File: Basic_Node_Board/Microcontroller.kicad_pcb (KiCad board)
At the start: 2 copper layers, 17 parts, among them J4 Conn_01x02_Pin, U2 ESP32-DEVKIT-C, U6 TJA1050T/CM,118

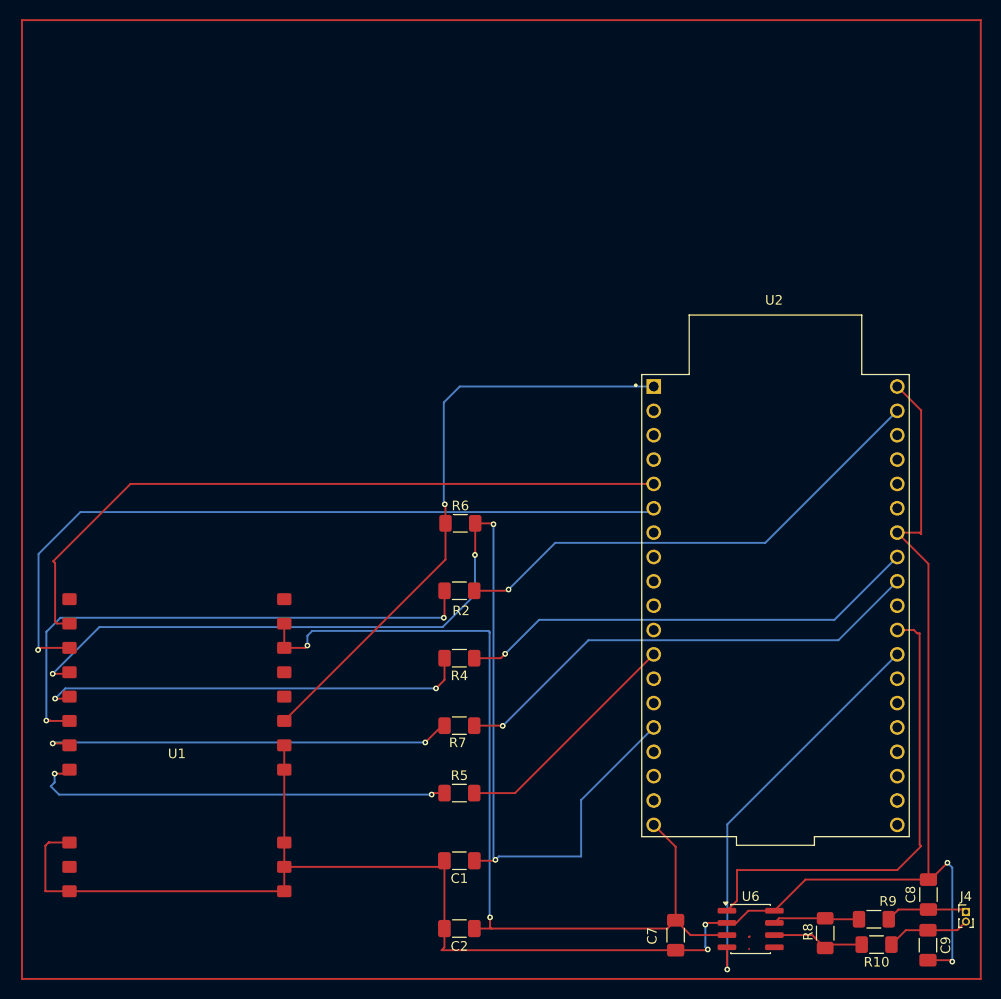
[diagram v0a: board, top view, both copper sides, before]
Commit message: microcontroller board without the buck converter yet
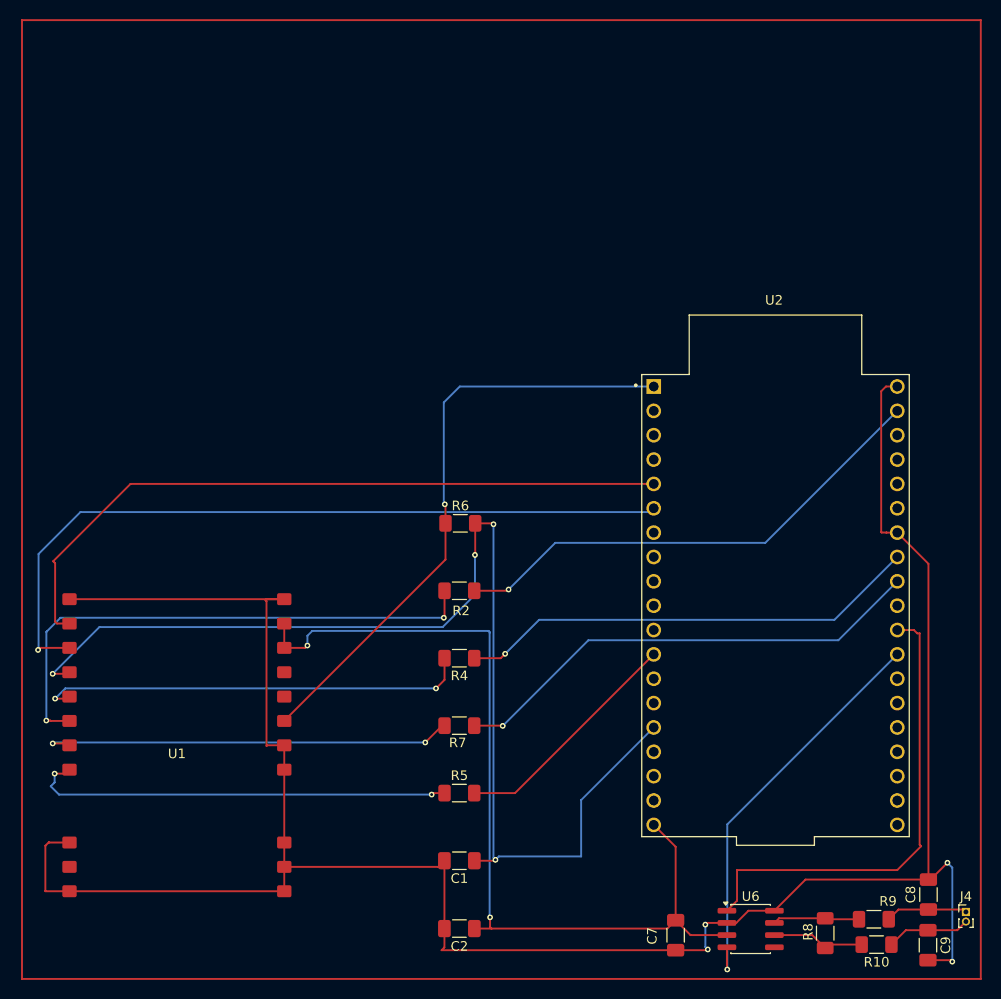
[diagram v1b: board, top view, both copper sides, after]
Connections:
- U1 pad 12: unconnected-(U1-GND-Pad12) -> GND
- U1 pad 7: unconnected-(U1-T/R_CTRL-Pad7) -> Net-(U1-DIO2)
- U1 pad 8: unconnected-(U1-DIO2-Pad8) -> Net-(U1-DIO2)
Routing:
- net GND: track 202.2 -> 243.1 mm

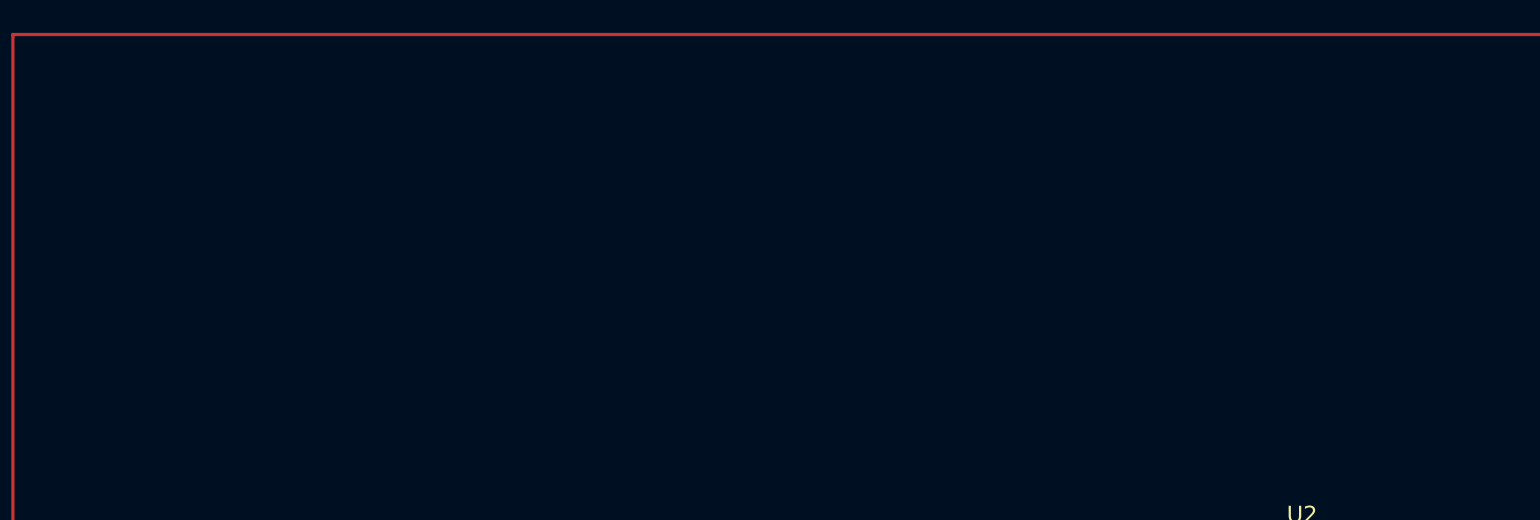
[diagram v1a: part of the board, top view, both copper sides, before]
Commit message: add buck buck converter step down to the pcb (not wirted yet)
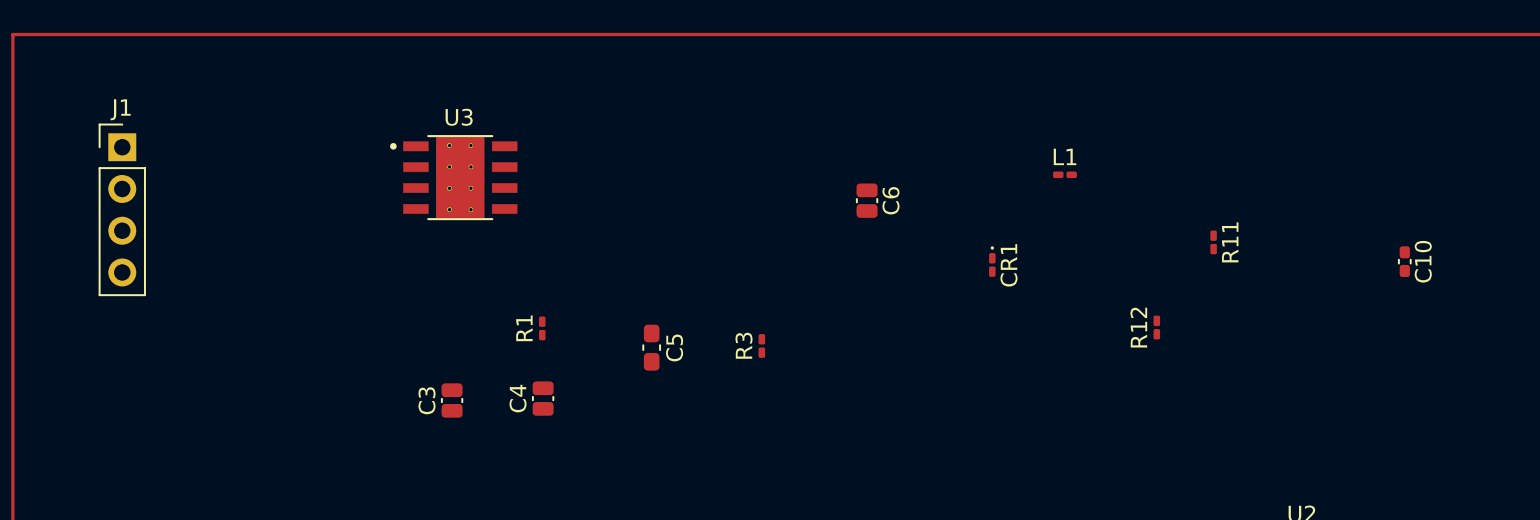
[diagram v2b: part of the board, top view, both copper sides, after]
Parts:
- added C10: 10TPE47MAZB, Capacitor_SMD:C_0402_1005Metric_Pad0.74x0.62mm_HandSolder, F.Cu at (120.2, 38.5)
- added C3: GRM31CR71H475KA12L, Capacitor_SMD:C_0504_1310Metric_Pad0.83x1.28mm_HandSolder, F.Cu at (62.2, 47.0)
- added C4: C0805C122J5GACTU, Capacitor_SMD:C_0504_1310Metric_Pad0.83x1.28mm_HandSolder, F.Cu at (67.8, 46.8)
- added C5: CL05C110JB5NNNC, Capacitor_SMD:C_0603_1608Metric_Pad1.08x0.95mm_HandSolder, F.Cu at (74.4, 43.7)
- added C6: 08053C104KAT2A, Capacitor_SMD:C_0504_1310Metric_Pad0.83x1.28mm_HandSolder, F.Cu at (87.5, 34.8)
- added CR1: B560C-13-F, Diode_SMD:D_0201_0603Metric_Pad0.64x0.40mm_HandSolder, F.Cu at (95.1, 38.7)
- added J1: Conn_01x02, Connector_PinHeader_2.54mm:PinHeader_1x04_P2.54mm_Vertical, F.Cu at (42.2, 31.5)
- added L1: SRN8040-100M, Inductor_SMD:L_0201_0603Metric_Pad0.64x0.40mm_HandSolder, F.Cu at (99.5, 33.2)
- added R1: RC0201FR-0723K7L, Resistor_SMD:R_0201_0603Metric_Pad0.64x0.40mm_HandSolder, F.Cu at (67.7, 42.6)
- added R11: CRCW040261K9FKED, Resistor_SMD:R_0201_0603Metric_Pad0.64x0.40mm_HandSolder, F.Cu at (108.6, 37.3)
- added R12: CRCW040211K0FKED, Resistor_SMD:R_0201_0603Metric_Pad0.64x0.40mm_HandSolder, F.Cu at (105.1, 42.5)
- added R3: CRCW0402118KFKED, Resistor_SMD:R_0201_0603Metric_Pad0.64x0.40mm_HandSolder, F.Cu at (81.1, 43.6)
- added U3: TPS54560BQDDARQ1, PROVE-footprints:VREG_LM5017MR_NOPB, F.Cu at (62.7, 33.4)

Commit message: beta test with all connections for final pcb layout - JK
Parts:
- added C11: 47uF, Capacitor_SMD:C_0402_1005Metric_Pad0.74x0.62mm_HandSolder, F.Cu at (79.9, 33.3)
- C10: value 10TPE47MAZB -> 47uF
- C3: value GRM31CR71H475KA12L -> 30uF
- C4: value C0805C122J5GACTU -> 82nF
- C5: value CL05C110JB5NNNC -> 100pF
- J1: footprint Connector_PinHeader_2.54mm:PinHeader_1x04_P2.54mm_Vertical -> Connector_PinHeader_1.00mm:PinHeader_1x02_P1.00mm_Vertical
- L1: value SRN8040-100M -> 47uH
- R1: value RC0201FR-0723K7L -> 5.1k
- R11: value CRCW040261K9FKED -> 10k
- R12: value CRCW040211K0FKED -> 56.2k
- R3: value CRCW0402118KFKED -> 243k
- moved J4 115.2 mm to (40.0, 51.0), turned to 180 degrees
- moved C9 111.1 mm to (46.9, 47.5), turned to 90 degrees
- moved C8 101.9 mm to (46.8, 57.1), turned to -90 degrees
- moved R10 101.3 mm to (52.5, 50.0), turned to 0 degrees
- moved R9 94.2 mm to (52.5, 57.5), turned to 0 degrees
- moved R8 91.4 mm to (57.6, 52.5), turned to 90 degrees
- moved U6 81.8 mm to (65.4, 51.9), turned to 180 degrees
- moved C7 73.1 mm to (75.0, 52.8)
- moved C10 44.2 mm to (76.3, 33.2)
- moved R3 30.7 mm to (52.5, 32.5)
- moved CR1 26.4 mm to (69.0, 34.5)
- moved C3 24.8 mm to (45.1, 29.1)
- moved C4 24.2 mm to (45.6, 37.3), turned to 0 degrees
- moved L1 23.8 mm to (76.0, 29.0), turned to 180 degrees
- moved C5 23.7 mm to (51.8, 36.5)
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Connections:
- C2 pad 1: /BUCK_5V -> 5.3V OUT
- C7 pad 2: /BUCK_5V -> 5.3V OUT
- R11 pad 1: 5.3V OUT -> Net-(U3-FB)
- R11 pad 2: Net-(U3-FB) -> GND
- R12 pad 1: GND -> Net-(U3-FB)
- R12 pad 2: Net-(U3-FB) -> 5.3V OUT
- U1 pad 10: /BUCK_5V -> 5.3V OUT
- U1 pad 9: /BUCK_5V -> 5.3V OUT
- U2 pad 19: /BUCK_5V -> 5.3V OUT
- U3 pad 3: unconnected-(U3-EN-Pad3) -> /24V
- U6 pad 3: /BUCK_5V -> 5.3V OUT
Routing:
- net GND: track 243.1 -> 422.2 mm, vias 4 -> 10
- net 5.3V OUT: track 0.00 -> 176.0 mm, vias 0 -> 4
- net /BUCK_5V: track 95.1 -> 0.00 mm, vias 2 -> 0
- net Net-(J3-Pin_12): track 42.5 -> 120.4 mm, vias 1 -> 0
- net Net-(J3-Pin_8): track 48.5 -> 94.2 mm
- net Net-(U3-FB): track 0.00 -> 31.2 mm, vias 0 -> 2
- net Net-(J3-Pin_9): track 50.4 -> 77.8 mm
- net Net-(U3-COMP): track 0.00 -> 23.9 mm
- net /24V: track 0.00 -> 22.0 mm
- net Net-(J2-Pin_5): track 73.9 -> 93.6 mm, vias 0 -> 2
- net Net-(U3-SW): track 0.00 -> 18.5 mm
- net Net-(J3-Pin_11): track 49.7 -> 65.5 mm, vias 0 -> 1
- net Net-(J2-Pin_12): track 24.7 -> 39.6 mm
- net Net-(J3-Pin_2): track 51.9 -> 65.9 mm
- net Net-(U3-BOOT): track 0.00 -> 12.2 mm
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- added copper zone on In1.Cu, net 5.3V OUT
- added copper zone on In2.Cu, net GND
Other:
- copper layers 2 -> 4

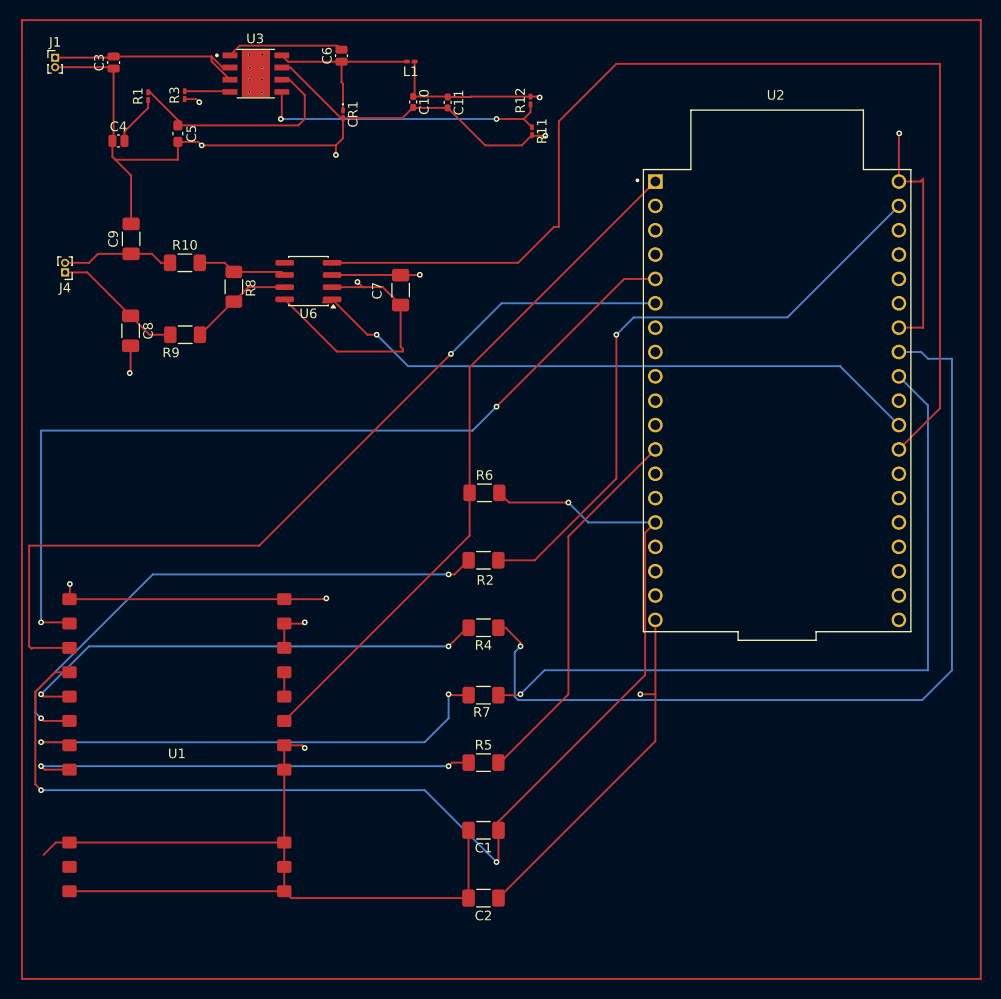
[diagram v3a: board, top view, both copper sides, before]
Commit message: revised e22P transceiver module footprint and began to add labels for the 3d Board design
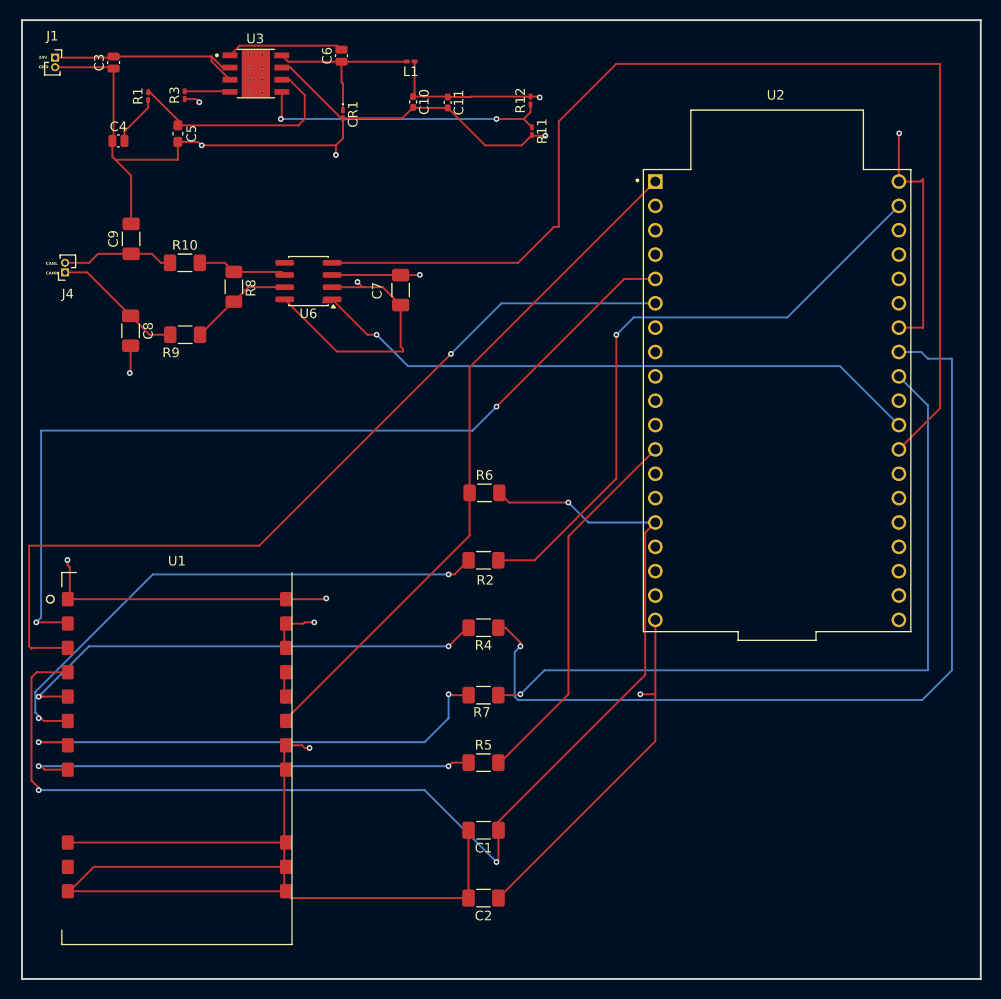
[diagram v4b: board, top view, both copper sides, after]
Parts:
- J1, J4: footprint Connector_PinHeader_1.00mm:PinHeader_1x02_P1.00mm_Vertical -> Connector_PinSocket_1.00mm:PinSocket_1x02_P1.00mm_Vertical
- U1: footprint Library:E22P-915M30S -> PROVE-footprints:E22P-915M30S_revised
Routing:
- net GND: track 422.2 -> 445.0 mm
- net Net-(J2-Pin_15): track 125.9 -> 127.3 mm
- net Net-(J2-Pin_5): track 93.6 -> 94.3 mm
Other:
- board outline added: 100 x 100 mm
- board text added: "24V"
- board text added: "CANH"
- board text added: "CANL"
- board text added: "GND"

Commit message: fixed routing under the lora board module
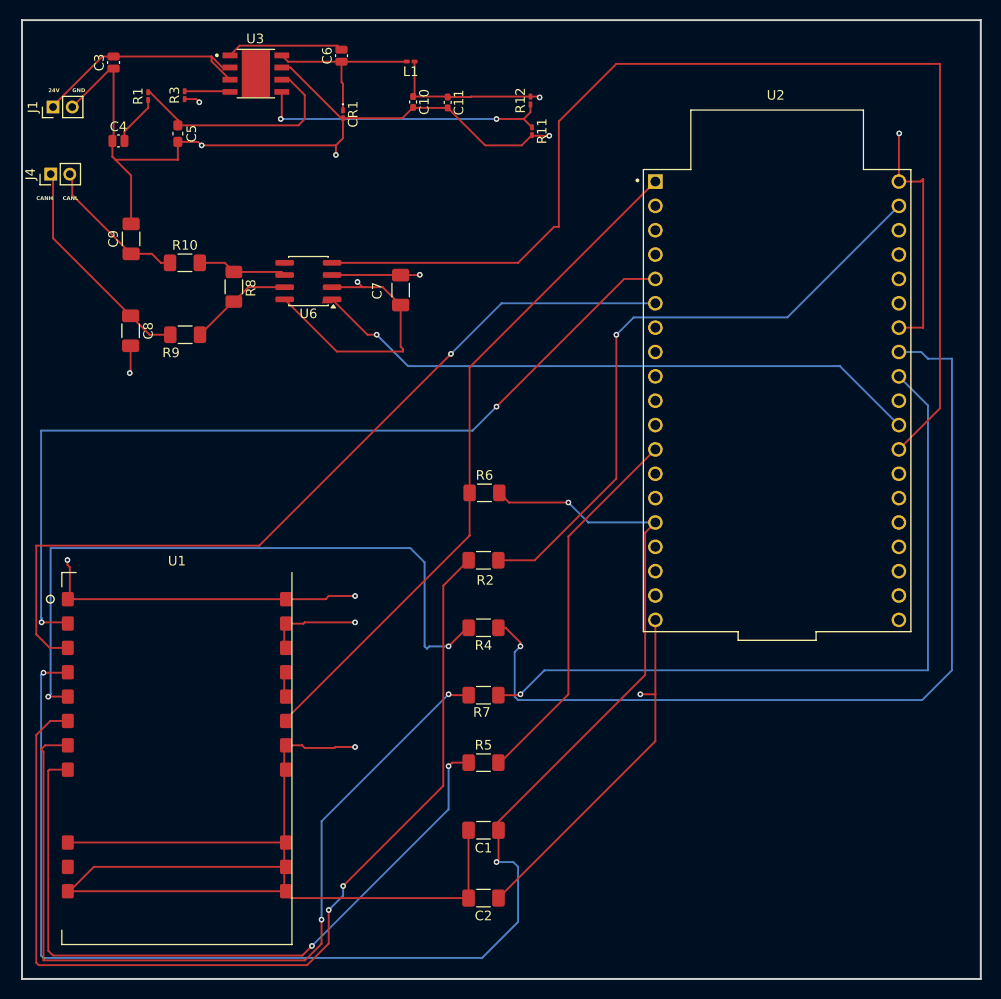
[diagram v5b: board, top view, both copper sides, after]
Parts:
- J1, J4: footprint Connector_PinSocket_1.00mm:PinSocket_1x02_P1.00mm_Vertical -> Connector_PinHeader_2.00mm:PinHeader_1x02_P2.00mm_Vertical
- moved J4 10.4 mm to (38.5, 40.8), turned to 90 degrees
- moved J1 5.15 mm to (38.8, 33.8), turned to 90 degrees
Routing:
- net Net-(U1-MOSI): track 57.0 -> 105.2 mm
- net Net-(U1-SCK): track 51.3 -> 88.9 mm
- net Net-(U1-NSS): track 48.4 -> 76.5 mm
- net Net-(J2-Pin_15): track 127.3 -> 152.2 mm
- net Net-(U1-MISO): track 51.0 -> 71.9 mm
- net GND: track 445.0 -> 456.4 mm
- net /CANH: track 13.7 -> 23.2 mm
- net /24V: track 22.0 -> 26.0 mm
- net /CANL: track 11.7 -> 15.4 mm
- net Net-(J2-Pin_6): track 90.6 -> 88.3 mm
- net Net-(J2-Pin_5): track 94.3 -> 93.6 mm

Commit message: small revisions before printing
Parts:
- moved R10 4.60 mm to (54.2, 45.8)
- moved R12 2.59 mm to (88.2, 30.5)
- moved R3 2.01 mm to (51.5, 30.8)
- moved R9 1.40 mm to (53.5, 58.5)
- moved R11 0.85 mm to (88.0, 36.8)
- moved J1 0.35 mm to (38.5, 33.5)
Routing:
- net GND: track 456.4 -> 463.1 mm
- net 5.3V OUT: track 176.0 -> 180.8 mm
- net Net-(U3-FB): track 31.2 -> 34.1 mm
- net /CANL: track 15.4 -> 18.1 mm
- net Net-(U6-CANL): track 9.38 -> 11.4 mm
- net Net-(U3-RT/CLK): track 4.75 -> 6.46 mm
- net /CANH: track 23.2 -> 24.6 mm
- net Net-(U6-CANH): track 10.9 -> 11.5 mm
